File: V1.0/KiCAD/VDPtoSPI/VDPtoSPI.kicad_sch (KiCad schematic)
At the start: 26 parts

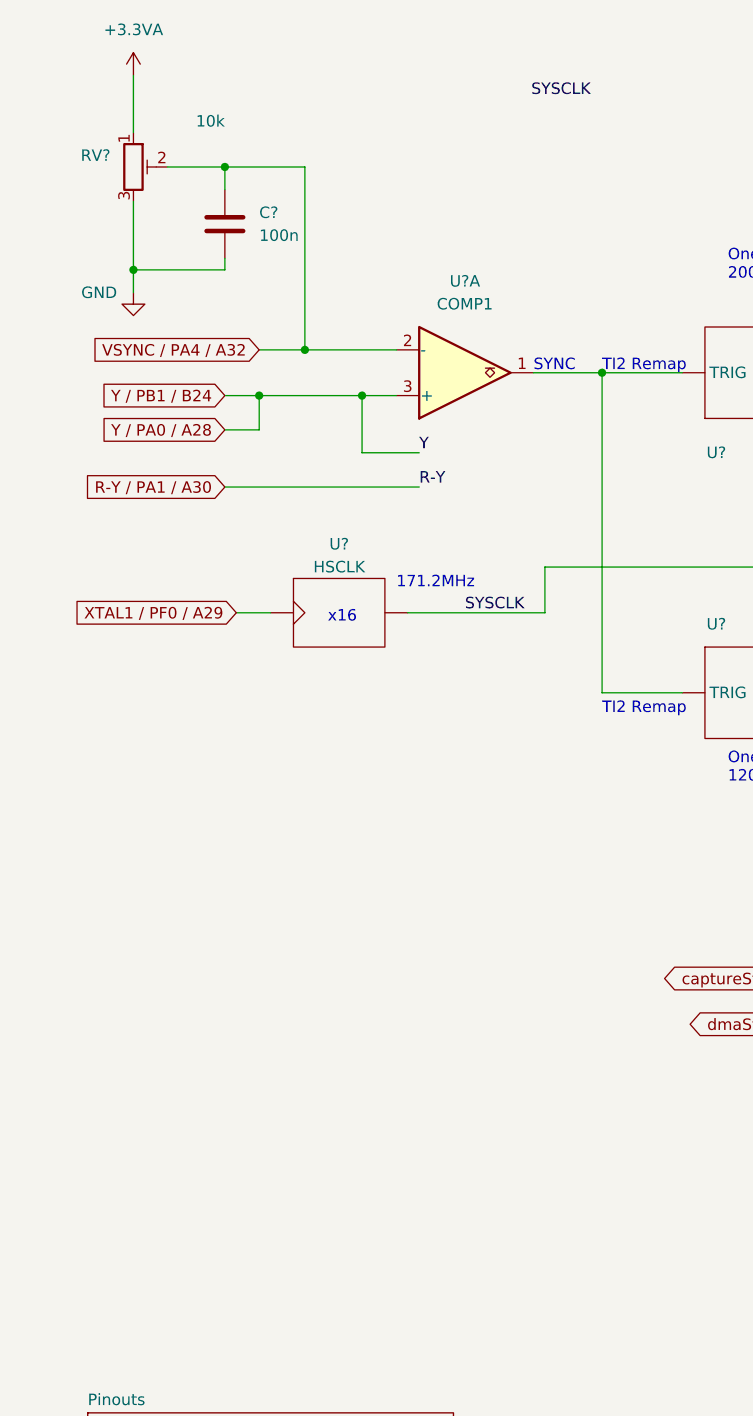
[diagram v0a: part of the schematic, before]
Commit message: README update and PCB outputs
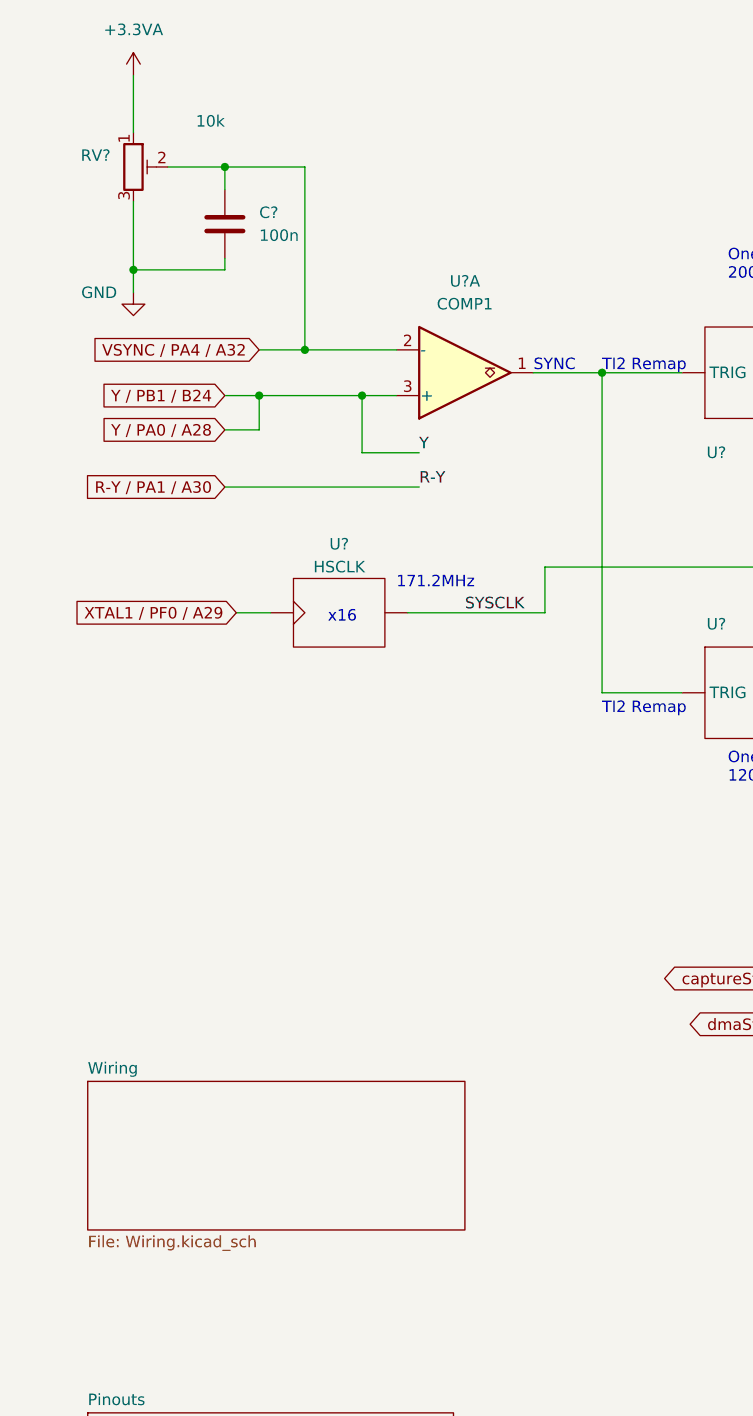
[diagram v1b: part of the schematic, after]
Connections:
- net at U?. (DIN): now also U?., U?. (DIN); no longer U?. (SCK)
- net at U?.: now also U?.; no longer U?. (DIN)
- net at U?. (TRIG): now also U?. (TRIG), U?.1; no longer U?.
- net at U?.: now also U?.; no longer U?.
- new net: U?. (DIN), U?. (SCK) (x2)
- new net: U?., U?. (SCK)
- new net: U?. (DIN), U?. (VIN), U?. (VIN)
- new net: U?. (DIN), U?. (VIN)
- new net: U?., U?. (DIN) (x3)
- new net: U?., U?. (TRIG)
- new net: U?. (TRIG), U?. (TRIG) (x2)
- new net: U?., U?.
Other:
- added sheet Wiring (Wiring.kicad_sch)
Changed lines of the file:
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@@
     (effects (font (size 1.27 1.27)) (justify left bottom))
-  )
-  (label "SYSCLK" (at 76.2 22.86 180)
-    (effects (font (size 1.27 1.27)) (justify right bottom))
   )
   (label "INT" (at 217.17 63.5 0)
@@
     )
   )
+  (sheet (at 20.32 132.08) (size 41.91 16.51) (fields_autoplaced)
+    (stroke (width 0.1524) (type solid) (color 0 0 0 0))
+    (fill (color 0 0 0 0.0000))
+    (property "Sheet name" "Wiring" (id 0) (at 20.32 131.3684 0)
+      (effects (font (size 1.27 1.27)) (justify left bottom))
+    )
+    (property "Sheet file" "Wiring.kicad_sch" (id 1) (at 20.32 149.1746 0)
+      (effects (font (size 1.27 1.27)) (justify left top))
+    )
+  )
   (sheet_instances
     (path "/" (page "1"))
     (path "/1929d1e9-1472-44d5-bb5a-6ba1c1c66e1c" (page "2"))
+    (path "/edcb695f-3c5d-4e62-80d2-e57589dd54c9" (page "3"))
   )
   (symbol_instances
@@
       (reference "#PWR?") (unit 1) (value "GND") (footprint "")
     )
+    (path "/edcb695f-3c5d-4e62-80d2-e57589dd54c9/10504469-e9c9-4fa5-818b-82c8ab6f8c88"
+      (reference "#PWR?") (unit 1) (value "GND") (footprint "")
+    )
+    (path "/edcb695f-3c5d-4e62-80d2-e57589dd54c9/147b2b77-5566-44a1-970c-0adaa967941b"
+      (reference "#PWR?") (unit 1) (value "GND") (footprint "")
+    )
+    (path "/edcb695f-3c5d-4e62-80d2-e57589dd54c9/18a30380-7e27-4832-994d-8a9e037ad28f"
+      (reference "#PWR?") (unit 1) (value "GND") (footprint "")
+    )
+    (path "/edcb695f-3c5d-4e62-80d2-e57589dd54c9/21400cdb-6945-4d82-8f5b-7233b89b6f72"
+      (reference "#PWR?") (unit 1) (value "GND") (footprint "")
+    )
+    (path "/edcb695f-3c5d-4e62-80d2-e57589dd54c9/2eac0a19-3313-44b7-aa29-6a6d49a5de93"
+      (reference "#PWR?") (unit 1) (value "GND") (footprint "")
+    )
+    (path "/edcb695f-3c5d-4e62-80d2-e57589dd54c9/3ec3d042-85d6-4cb7-8668-d0f192bb6282"
+      (reference "#PWR?") (unit 1) (value "GND") (footprint "")
+    )
+    (path "/edcb695f-3c5d-4e62-80d2-e57589dd54c9/4b3b36e5-8cae-4e1c-a802-e1a7ab60c1aa"
+      (reference "#PWR?") (unit 1) (value "GND") (footprint "")
+    )
+    (path "/edcb695f-3c5d-4e62-80d2-e57589dd54c9/5ade870f-3654-4b41-935e-891408a93d0c"
+      (reference "#PWR?") (unit 1) (value "GND") (footprint "")
+    )
     (path "/72db6e2d-deb4-46b1-a3af-9de172436885"
       (reference "#PWR?") (unit 1) (value "+3.3VA") (footprint "")
     )
+    (path "/edcb695f-3c5d-4e62-80d2-e57589dd54c9/877cfe79-ce71-4914-993c-d95826424267"
+      (reference "#PWR?") (unit 1) (value "+3.3V") (footprint "")
+    )
+    (path "/edcb695f-3c5d-4e62-80d2-e57589dd54c9/a3289c09-982f-4ccb-9a23-d8497baf0be1"
+      (reference "#PWR?") (unit 1) (value "+3.3V") (footprint "")
+    )
+    (path "/edcb695f-3c5d-4e62-80d2-e57589dd54c9/bef002fa-e90b-4924-9921-93bed373aede"
+      (reference "#PWR?") (unit 1) (value "+3.3V") (footprint "")
+    )
+    (path "/edcb695f-3c5d-4e62-80d2-e57589dd54c9/c31673e9-6536-429b-999f-54766bbabc9f"
+      (reference "#PWR?") (unit 1) (value "GND") (footprint "")
+    )
+    (path "/edcb695f-3c5d-4e62-80d2-e57589dd54c9/c5bc367c-11fa-4a03-a3d6-0ffd6b340f74"
+      (reference "#PWR?") (unit 1) (value "GND") (footprint "")
+    )
+    (path "/edcb695f-3c5d-4e62-80d2-e57589dd54c9/f700dcec-07db-4694-a2b3-f727ad8488b8"
+      (reference "#PWR?") (unit 1) (value "+3.3VA") (footprint "")
+    )
+    (path "/edcb695f-3c5d-4e62-80d2-e57589dd54c9/fb259233-3c44-4412-99f6-690232db0af7"
+      (reference "#PWR?") (unit 1) (value "GND") (footprint "")
+    )
+    (path "/edcb695f-3c5d-4e62-80d2-e57589dd54c9/fb6f2c21-c915-477d-b5cf-151e07b459d3"
+      (reference "#PWR?") (unit 1) (value "GND") (footprint "")
+    )
+    (path "/edcb695f-3c5d-4e62-80d2-e57589dd54c9/fb906165-c827-4154-b3bb-ed1fe0a4d0eb"
+      (reference "#PWR?") (unit 1) (value "GND") (footprint "")
+    )
+    (path "/edcb695f-3c5d-4e62-80d2-e57589dd54c9/fd47311d-aae7-4659-ad2c-ed81281f8e89"
+      (reference "#PWR?") (unit 1) (value "GND") (footprint "")
+    )
+    (path "/edcb695f-3c5d-4e62-80d2-e57589dd54c9/3209bef1-b9fe-4055-ac99-3b07a9abd868"
+      (reference "C?") (unit 1) (value "100n") (footprint "Capacitor_SMD:C_0805_2012Metric")
+    )
+    (path "/edcb695f-3c5d-4e62-80d2-e57589dd54c9/3372042d-cc47-4946-8fc1-664f70e0516a"
+      (reference "C?") (unit 1) (value "4u7") (footprint "Capacitor_SMD:C_0805_2012Metric")
+    )
+    (path "/edcb695f-3c5d-4e62-80d2-e57589dd54c9/337b3416-36a2-448c-a464-e84d585cddc9"
+      (reference "C?") (unit 1) (value "4u7") (footprint "Capacitor_SMD:C_0805_2012Metric")
+    )
+    (path "/edcb695f-3c5d-4e62-80d2-e57589dd54c9/9ba580e5-3ed6-45c4-9341-94eeb02a223b"
+      (reference "C?") (unit 1) (value "100n") (footprint "")
+    )
+    (path "/edcb695f-3c5d-4e62-80d2-e57589dd54c9/b96d6d36-367c-4433-99f1-0ab5949f2988"
+      (reference "C?") (unit 1) (value "100n") (footprint "Capacitor_SMD:C_0805_2012Metric")
+    )
     (path "/ba809679-b477-462e-b9db-2a17ef680337"
       (reference "C?") (unit 1) (value "100n") (footprint "")
     )
+    (path "/edcb695f-3c5d-4e62-80d2-e57589dd54c9/14e68f1d-e5b1-432f-9b77-727e9889c607"
+      (reference "J?") (unit 1) (value "Conn_02x19_Odd_Even") (footprint "")
+    )
+    (path "/edcb695f-3c5d-4e62-80d2-e57589dd54c9/3c8014bd-6e02-4c4b-9719-19bfebd24c58"
+      (reference "J?") (unit 1) (value "Conn_02x19_Odd_Even") (footprint "")
+    )
+    (path "/edcb695f-3c5d-4e62-80d2-e57589dd54c9/ac6800cc-787c-487f-8163-33eaa1378b96"
+      (reference "J?") (unit 1) (value "TFT Parallel Port") (footprint "Connector_PinHeader_2.54mm:PinHeader_2x16_P2.54mm_Vertical")
+    )
+    (path "/edcb695f-3c5d-4e62-80d2-e57589dd54c9/ac6f255e-3c5e-4565-8bdb-29a0542598c6"
+      (reference "J?") (unit 1) (value "TFT SPI Port") (footprint "Connector_PinHeader_2.54mm:PinHeader_2x04_P2.54mm_Vertical")
+    )
+    (path "/edcb695f-3c5d-4e62-80d2-e57589dd54c9/4b85f311-d790-4802-a0df-aeb3dbc3232a"
+      (reference "R?") (unit 1) (value "3K9") (footprint "Resistor_SMD:R_0805_2012Metric_Pad1.20x1.40mm_HandSolder")
+    )
     (path "/88af8049-06a5-43e3-af0e-09209eb1b1fc"
       (reference "RV?") (unit 1) (value "10k") (footprint "")
     )
+    (path "/edcb695f-3c5d-4e62-80d2-e57589dd54c9/cb7a145d-8dc8-40c4-bba9-0a71fe5d9fc4"
+      (reference "RV?") (unit 1) (value "10K") (footprint "")
+    )
+    (path "/edcb695f-3c5d-4e62-80d2-e57589dd54c9/dbabf690-5cdb-41c3-885e-f55bce0c8cd4"
+      (reference "SW?") (unit 1) (value "RotaryEncoder_Switch") (footprint "")
+    )
     (path "/08821279-27d1-4758-b48e-622cd204109c"
       (reference "U?") (unit 1) (value "SPI") (footprint "")
@@
       (reference "U?") (unit 1) (value "SPICLK") (footprint "")
     )
+    (path "/edcb695f-3c5d-4e62-80d2-e57589dd54c9/3ae4ea5f-2225-43e0-892f-a657940ac0af"
+      (reference "U?") (unit 1) (value "TMS9128") (footprint "")
+    )
     (path "/3d2d0803-ab1a-4a1e-bdbe-18e17b4e9c0e"
